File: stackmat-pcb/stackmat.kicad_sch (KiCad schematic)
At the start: 12 parts, among them J1 LCD, J2 RFID, J3 DBG_SERIAL, J4 JACK_MALE, J5 JACK_FEMALE, J7 BTN, J8 Screw_Terminal_01x02, J9 POWER_SW, U1 ESP-12F/E, U2 18650, U3 AMS1117-3.3

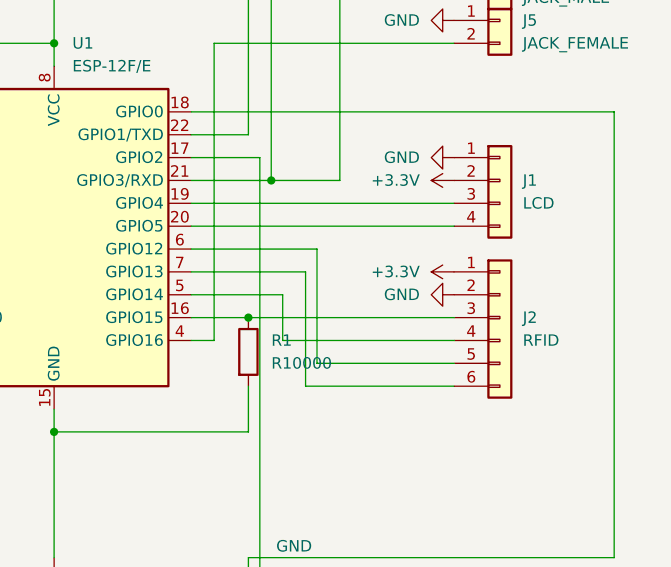
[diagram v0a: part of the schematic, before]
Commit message: chore: kikit panelizer
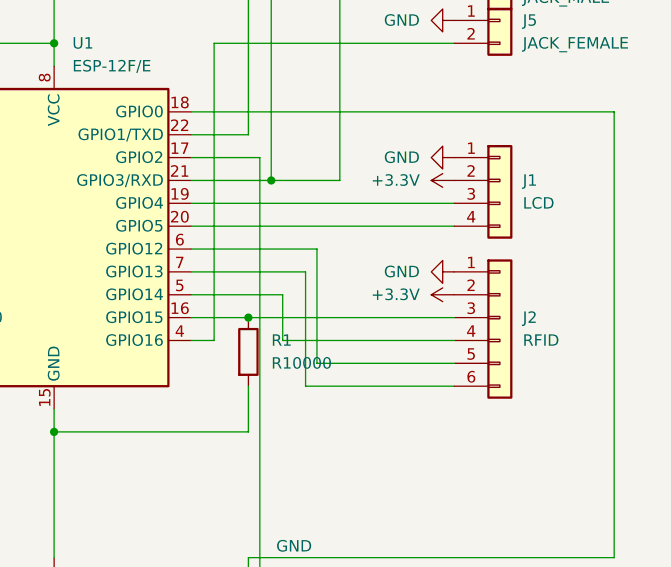
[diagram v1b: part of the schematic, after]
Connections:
- net +3.3V: now also J2.2 (Pin_2); no longer J2.1 (Pin_1)
- net GND: now also J2.1 (Pin_1); no longer J2.2 (Pin_2)
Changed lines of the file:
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@@
     (pin "3")
   )
-  (symbol (lib_id "power:GND") (at 185.42 96.52 270) (unit 1)
+  (symbol (lib_id "power:GND") (at 185.42 93.98 270) (unit 1)
     (in_bom yes) (on_board yes) (fields_autoplaced)
-    (property "Reference" "#PWR0104" (id 0) (at 179.07 96.52 0)
+    (property "Reference" "#PWR0104" (id 0) (at 179.07 93.98 0)
       (effects (font (size 1.27 1.27)) hide)
     )
-    (property "Value" "GND" (id 1) (at 181.61 96.5199 90)
+    (property "Value" "GND" (id 1) (at 181.61 93.9799 90)
       (effects (font (size 1.27 1.27)) (justify right))
+    )
+    (property "Footprint" "" (id 2) (at 185.42 93.98 0)
+      (effects (font (size 1.27 1.27)) hide)
+    )
+    (property "Datasheet" "" (id 3) (at 185.42 93.98 0)
+      (effects (font (size 1.27 1.27)) hide)
+    )
+    (pin "1")
+  )
+  (symbol (lib_id "power:+3.3V") (at 185.42 96.52 90) (unit 1)
+    (in_bom yes) (on_board yes) (fields_autoplaced)
+    (property "Reference" "#PWR0106" (id 0) (at 189.23 96.52 0)
+      (effects (font (size 1.27 1.27)) hide)
+    )
+    (property "Value" "+3.3V" (id 1) (at 181.61 96.5199 90)
+      (effects (font (size 1.27 1.27)) (justify left))
     )
     (property "Footprint" "" (id 2) (at 185.42 96.52 0)
@@
       (effects (font (size 1.27 1.27)) hide)
     )
-    (pin "1")
-  )
-  (symbol (lib_id "power:+3.3V") (at 185.42 93.98 90) (unit 1)
-    (in_bom yes) (on_board yes) (fields_autoplaced)
-    (property "Reference" "#PWR0106" (id 0) (at 189.23 93.98 0)
-      (effects (font (size 1.27 1.27)) hide)
-    )
-    (property "Value" "+3.3V" (id 1) (at 181.61 93.9799 90)
-      (effects (font (size 1.27 1.27)) (justify left))
-    )
-    (property "Footprint" "" (id 2) (at 185.42 93.98 0)
-      (effects (font (size 1.27 1.27)) hide)
-    )
-    (property "Datasheet" "" (id 3) (at 185.42 93.98 0)
-      (effects (font (size 1.27 1.27)) hide)
-    )

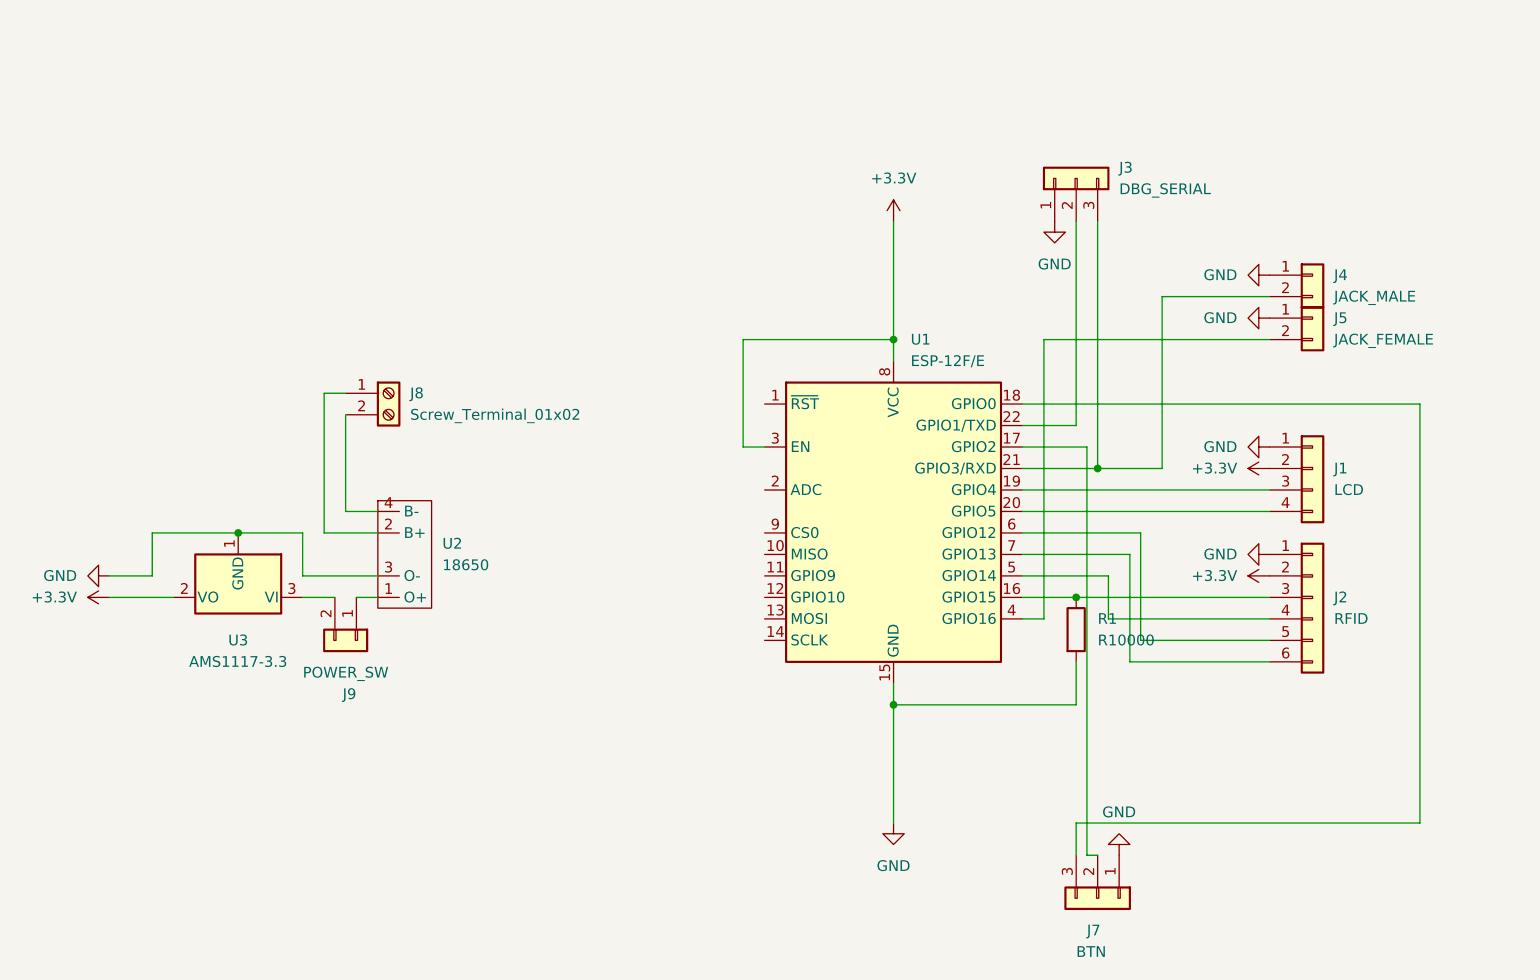
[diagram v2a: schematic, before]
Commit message: feat: submit time button (with pcb changes)
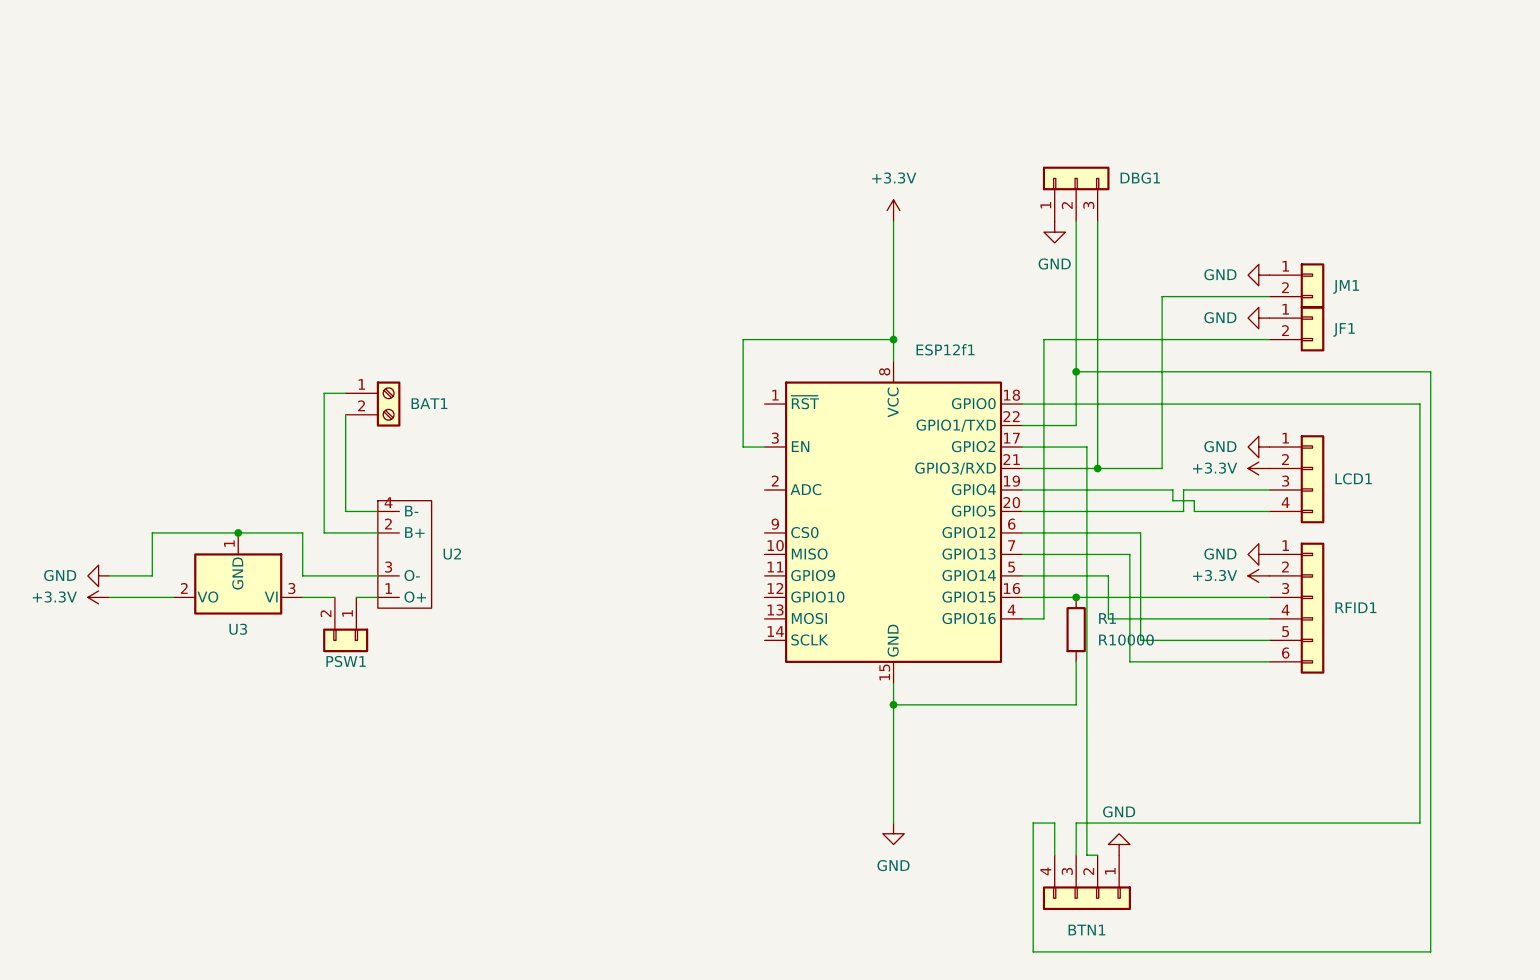
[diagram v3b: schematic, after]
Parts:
- removed J7: BTN, Connector_PinHeader_2.54mm:PinHeader_1x03_P2.54mm_Vertical, symbol Connector_Generic:Conn_01x03
- added BTN1: Conn_01x04, Connector_PinHeader_2.54mm:PinHeader_1x04_P2.54mm_Vertical, symbol Connector_Generic:Conn_01x04
- renumbered J8 to BAT1, J3 to DBG1, U1 to ESP12f1, J5 to JF1, J4 to JM1, J1 to LCD1, J9 to PSW1, J2 to RFID1
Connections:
- net GND: now also BTN1.1 (Pin_1)
- net at ESP12f1.17 (GPIO2): now also BTN1.2 (Pin_2)
- net at ESP12f1.18 (GPIO0): now also BTN1.3 (Pin_3)
- net at ESP12f1.19 (GPIO4): now also LCD1.4 (Pin_4); no longer LCD1.3 (Pin_3)
- net at ESP12f1.20 (GPIO5): now also LCD1.3 (Pin_3); no longer LCD1.4 (Pin_4)
- net at DBG1.2 (Pin_2), ESP12f1.22 (GPIO1/TXD): now also BTN1.4 (Pin_4)

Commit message: feat(pcb): smaller size (for 2x3 pannels)
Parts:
- DBG1: footprint Connector_PinHeader_2.54mm:PinHeader_1x03_P2.54mm_Vertical -> Connector_PinHeader_2.00mm:PinHeader_1x03_P2.00mm_Vertical
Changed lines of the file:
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@@
       (effects (font (size 1.27 1.27)) (justify right) hide)
     )
-    (property "Footprint" "Connector_PinHeader_2.54mm:PinHeader_1x03_P2.54mm_Vertical" (at 162.56 49.53 0)
+    (property "Footprint" "Connector_PinHeader_2.00mm:PinHeader_1x03_P2.00mm_Vertical" (at 162.56 49.53 0)
       (effects (font (size 1.27 1.27)) hide)
     )

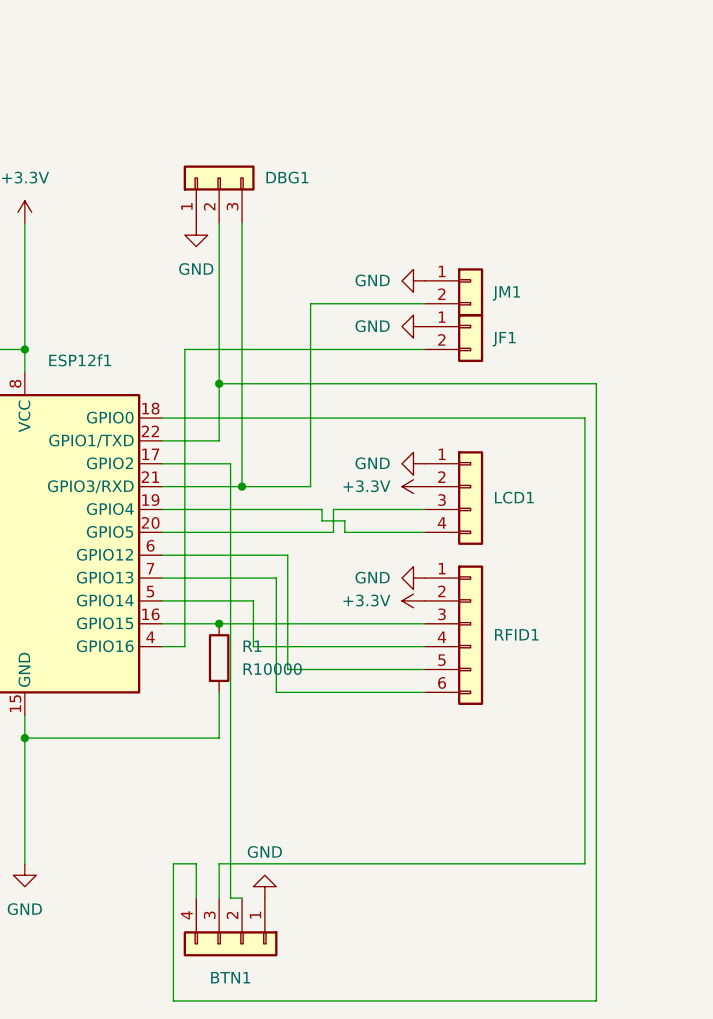
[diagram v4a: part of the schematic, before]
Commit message: wip(pcb): transistors instead of serial "copy"
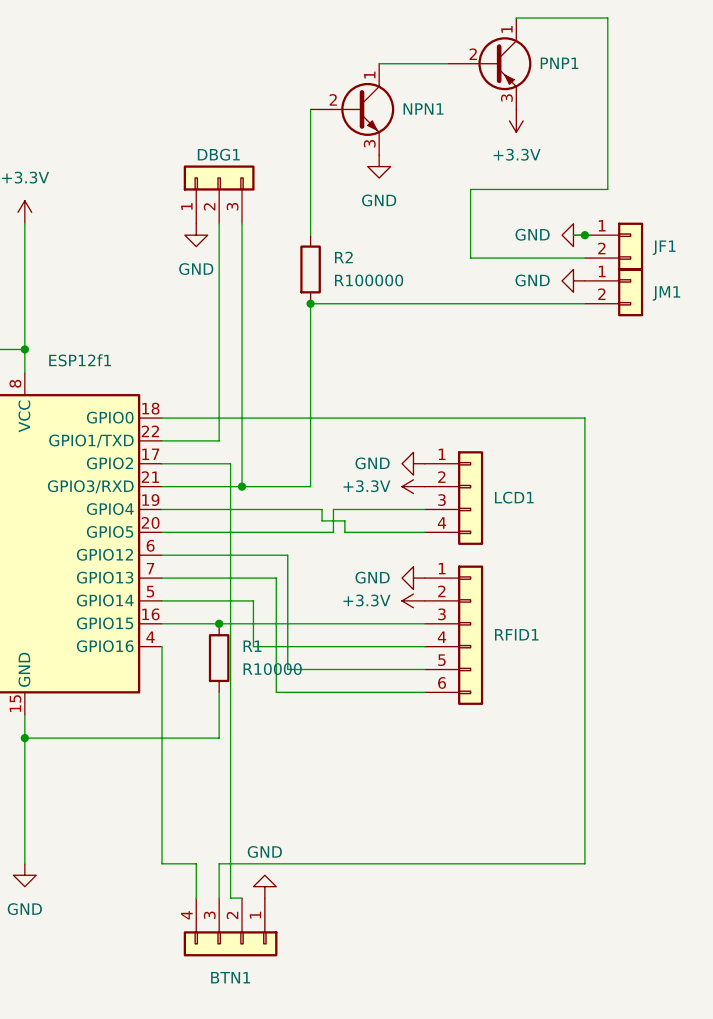
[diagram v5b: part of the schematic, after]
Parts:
- added NPN1: BC337, Package_TO_SOT_THT:TO-92_Inline, symbol Transistor_BJT:BC337
- added PNP1: BC557, Package_TO_SOT_THT:TO-92_Inline, symbol Transistor_BJT:BC557
- added R2: R100000, Resistor_THT:R_Axial_DIN0204_L3.6mm_D1.6mm_P7.62mm_Horizontal, symbol Device:R
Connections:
- net +3.3V: now also PNP1.3 (E)
- net GND: now also NPN1.3 (E)
- net at DBG1.3 (Pin_3), ESP12f1.21 (GPIO3/RXD), JM1.2 (Pin_2): now also R2.2
- net at DBG1.2 (Pin_2), ESP12f1.22 (GPIO1/TXD): no longer BTN1.4 (Pin_4)
- net at ESP12f1.4 (GPIO16): now also BTN1.4 (Pin_4); no longer JF1.2 (Pin_2)
- new net: NPN1.1 (C), PNP1.2 (B)
- new net: NPN1.2 (B), R2.1
- new net: JF1.2 (Pin_2), PNP1.1 (C)
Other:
- moved on the sheet: JF1, JM1

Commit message: feat(pcb): one transistor design
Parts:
- removed BTN1: Conn_01x04, Connector_PinHeader_2.54mm:PinHeader_1x04_P2.54mm_Vertical, symbol Connector_Generic:Conn_01x04
- removed PNP1: BC557, Package_TO_SOT_THT:TO-92_Inline, symbol Transistor_BJT:BC557
- added BTN1: Conn_01x03, Connector_PinHeader_2.54mm:PinHeader_1x03_P2.54mm_Vertical, symbol Connector_Generic:Conn_01x03
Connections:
- net +3.3V: now also NPN1.1 (C)
- net GND: now also BTN1.1 (Pin_1); no longer NPN1.3 (E)
- net at ESP12f1.17 (GPIO2): now also BTN1.2 (Pin_2)
- net at ESP12f1.18 (GPIO0): now also BTN1.3 (Pin_3)
- net at JF1.2 (Pin_2): now also NPN1.3 (E)
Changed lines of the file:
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@@
-    (stroke (width 0) (type default))
-  )
-  (wire (pts (xy 195.58 31.75) (xy 205.74 31.75))
     (stroke (width 0) (type default))
   )
@@
     (stroke (width 0) (type default))
   )
-  (wire (pts (xy 190.5 50.8) (xy 190.5 58.42))
-    (stroke (width 0) (type default))
-  )
-  (wire (pts (xy 205.74 50.8) (xy 190.5 50.8))
-    (stroke (width 0) (type default))
-  )
   (wire (pts (xy 53.34 91.44) (xy 53.34 96.52))
     (stroke (width 0) (type default))
@@
     (stroke (width 0) (type default))
   )
-  (wire (pts (xy 156.21 125.73) (xy 160.02 125.73))
-    (stroke (width 0) (type default))
-  )
   (wire (pts (xy 166.37 101.6) (xy 166.37 96.52))
     (stroke (width 0) (type default))
@@
     (stroke (width 0) (type default))
   )
-  (wire (pts (xy 190.5 58.42) (xy 203.2 58.42))
+  (wire (pts (xy 180.34 58.42) (xy 203.2 58.42))
     (stroke (width 0) (type default))
   )
@@
     (stroke (width 0) (type default))
   )
+  (wire (pts (xy 180.34 46.99) (xy 180.34 58.42))
+    (stroke (width 0) (type default))
+  )
   (wire (pts (xy 77.47 99.06) (xy 80.01 99.06))
     (stroke (width 0) (type default))
@@
     (stroke (width 0) (type default))
   )
-  (wire (pts (xy 160.02 129.54) (xy 160.02 125.73))
-    (stroke (width 0) (type default))
-  )
   (wire (pts (xy 173.99 86.36) (xy 173.99 87.63))
     (stroke (width 0) (type default))
@@
     (stroke (width 0) (type default))
   )
-  (wire (pts (xy 156.21 101.6) (xy 156.21 125.73))
-    (stroke (width 0) (type default))
-  )
   (wire (pts (xy 172.72 63.5) (xy 203.2 63.5))
     (stroke (width 0) (type default))
@@
     (stroke (width 0) (type default))
   )
-  (wire (pts (xy 180.34 36.83) (xy 187.96 36.83))
-    (stroke (width 0) (type default))
-  )
   (wire (pts (xy 166.37 96.52) (xy 156.21 96.52))
     (stroke (width 0) (type default))
@@
   )
   (wire (pts (xy 165.1 83.82) (xy 172.72 83.82))
-    (stroke (width 0) (type default))
-  )
-  (wire (pts (xy 205.74 31.75) (xy 205.74 50.8))
     (stroke (width 0) (type default))
   )
@@
     )
   )
+  (symbol (lib_id "power:+3.3V") (at 180.34 36.83 0) (unit 1)
+    (in_bom yes) (on_board yes) (dnp no) (fields_autoplaced)
+    (property "Reference" "#PWR01" (at 180.34 40.64 0)
+      (effects (font (size 1.27 1.27)) hide)
+    )
+    (property "Value" "+3.3V" (at 180.34 31.75 0)
+      (effects (font (size 1.27 1.27)))
+    )
+    (property "Footprint" "" (at 180.34 36.83 0)
+      (effects (font (size 1.27 1.27)) hide)
+    )
+    (property "Datasheet" "" (at 180.34 36.83 0)
+      (effects (font (size 1.27 1.27)) hide)
+    )
+    (pin "1")
+    (instances
+      (project "stackmat"
+        (path "/ccd0dcac-df1d-4089-8f7e-e62a3e2f6f2a"
+          (reference "#PWR01") (unit 1)
+        )
+      )
+    )
+  )
   (symbol (lib_id "Transistor_BJT:BC337") (at 177.8 41.91 0) (unit 1)
     (in_bom yes) (on_board yes) (dnp no)
@@
         (path "/ccd0dcac-df1d-4089-8f7e-e62a3e2f6f2a"
           (reference "#PWR0110") (unit 1)
-        )
-      )
-    )
-  )
-  (symbol (lib_id "power:GND") (at 180.34 46.99 0) (unit 1)
-    (in_bom yes) (on_board yes) (dnp no) (fields_autoplaced)
-    (property "Reference" "#PWR01" (at 180.34 53.34 0)
-      (effects (font (size 1.27 1.27)) hide)
-    )
-    (property "Value" "GND" (at 180.34 52.07 0)
-      (effects (font (size 1.27 1.27)))
-    )
-    (property "Footprint" "" (at 180.34 46.99 0)
-      (effects (font (size 1.27 1.27)) hide)
-    )
-    (property "Datasheet" "" (at 180.34 46.99 0)
-      (effects (font (size 1.27 1.27)) hide)
-    )
-    (pin "1")
-    (instances
-      (project "stackmat"
-        (path "/ccd0dcac-df1d-4089-8f7e-e62a3e2f6f2a"
-          (reference "#PWR01") (unit 1)
         )
       )
@@
     )
   )
-  (symbol (lib_id "power:+3.3V") (at 195.58 41.91 180) (unit 1)
-    (in_bom yes) (on_board yes) (dnp no) (fields_autoplaced)
-    (property "Reference" "#PWR02" (at 195.58 38.1 0)
-      (effects (font (size 1.27 1.27)) hide)
-    )
-    (property "Value" "+3.3V" (at 195.58 46.99 0)
-      (effects (font (size 1.27 1.27)))
-    )
-    (property "Footprint" "" (at 195.58 41.91 0)
-      (effects (font (size 1.27 1.27)) hide)
-    )
-    (property "Datasheet" "" (at 195.58 41.91 0)
-      (effects (font (size 1.27 1.27)) hide)
-    )
-    (pin "1")
-    (instances
-      (project "stackmat"
-        (path "/ccd0dcac-df1d-4089-8f7e-e62a3e2f6f2a"
-          (reference "#PWR02") (unit 1)
-        )
-      )
-    )
-  )
-  (symbol (lib_id "Connector_Generic:Conn_01x04") (at 165.1 134.62 270) (unit 1)
-    (in_bom yes) (on_board yes) (dnp no) (fields_autoplaced)
-    (property "Reference" "BTN1" (at 163.83 138.43 90)
-      (effects (font (size 1.27 1.27)))
-    )
-    (property "Value" "Conn_01x04" (at 163.83 140.97 90)
-      (effects (font (size 1.27 1.27)) hide)
-    )
-    (property "Footprint" "Connector_PinHeader_2.54mm:PinHeader_1x04_P2.54mm_Vertical" (at 165.1 134.62 0)
+  (symbol (lib_id "Connector_Generic:Conn_01x03") (at 165.1 134.62 270) (unit 1)
+    (in_bom yes) (on_board yes) (dnp no)
+    (property "Reference" "BTN1" (at 162.56 137.16 90)
+      (effects (font (size 1.27 1.27)) (justify left))
+    )
+    (property "Value" "Conn_01x03" (at 170.18 135.89 90)
+      (effects (font (size 1.27 1.27)) (justify left))
+    )
+    (property "Footprint" "Connector_PinHeader_2.54mm:PinHeader_1x03_P2.54mm_Vertical" (at 165.1 134.62 0)
       (effects (font (size 1.27 1.27)) hide)
     )
@@
       (effects (font (size 1.27 1.27)) hide)
     )
-    (pin "4")
-    (pin "2")
     (pin "3")
+    (pin "2")
     (pin "1")
     (instances
@@
         )
       )
-    )
-  )
-  (symbol (lib_id "Transistor_BJT:BC557") (at 193.04 36.83 0) (unit 1)
-    (in_bom yes) (on_board yes) (dnp no)
-    (property "Reference" "PNP1" (at 198.12 36.83 0)
-      (effects (font (size 1.27 1.27)) (justify left))
-    )
-    (property "Value" "BC557" (at 198.12 38.1 0)
-      (effects (font (size 1.27 1.27)) (justify left) hide)
-    )
-    (property "Footprint" "Package_TO_SOT_THT:TO-92_Inline" (at 198.12 38.735 0)
-      (effects (font (size 1.27 1.27) italic) (justify left) hide)
-    )
-    (property "Datasheet" "https://www.onsemi.com/pub/Collateral/BC556BTA-D.pdf" (at 193.04 36.83 0)
-      (effects (font (size 1.27 1.27)) (justify left) hide)
-    )
-    (pin "3")
-    (pin "2")
-    (pin "1")
-    (instances
-      (project "stackmat"
-        (path "/ccd0dcac-df1d-4089-8f7e-e62a3e2f6f2a"
-          (reference "PNP1") (unit 1)
-        )
-      )
